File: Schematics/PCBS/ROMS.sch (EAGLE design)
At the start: 4 parts, among them IC1 ATMEGA328P-AU, Y1 16MHz

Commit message: working on VCC power
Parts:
- added R1: 10K, adafruit:R-US_0207/10
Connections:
- new net N$3: IC1.PC6_[RESET/PCINT14], R1.1
- new net VCC: IC1.AVCC, IC1.VCC_1, IC1.VCC_2, R1.2
- net GND: now also C1.2, IC1.GND_1, IC1.GND_2, IC1.GND_3; no longer C1.1
- net N$1: now also C1.1; no longer C1.2
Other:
- moved on the sheet: C1

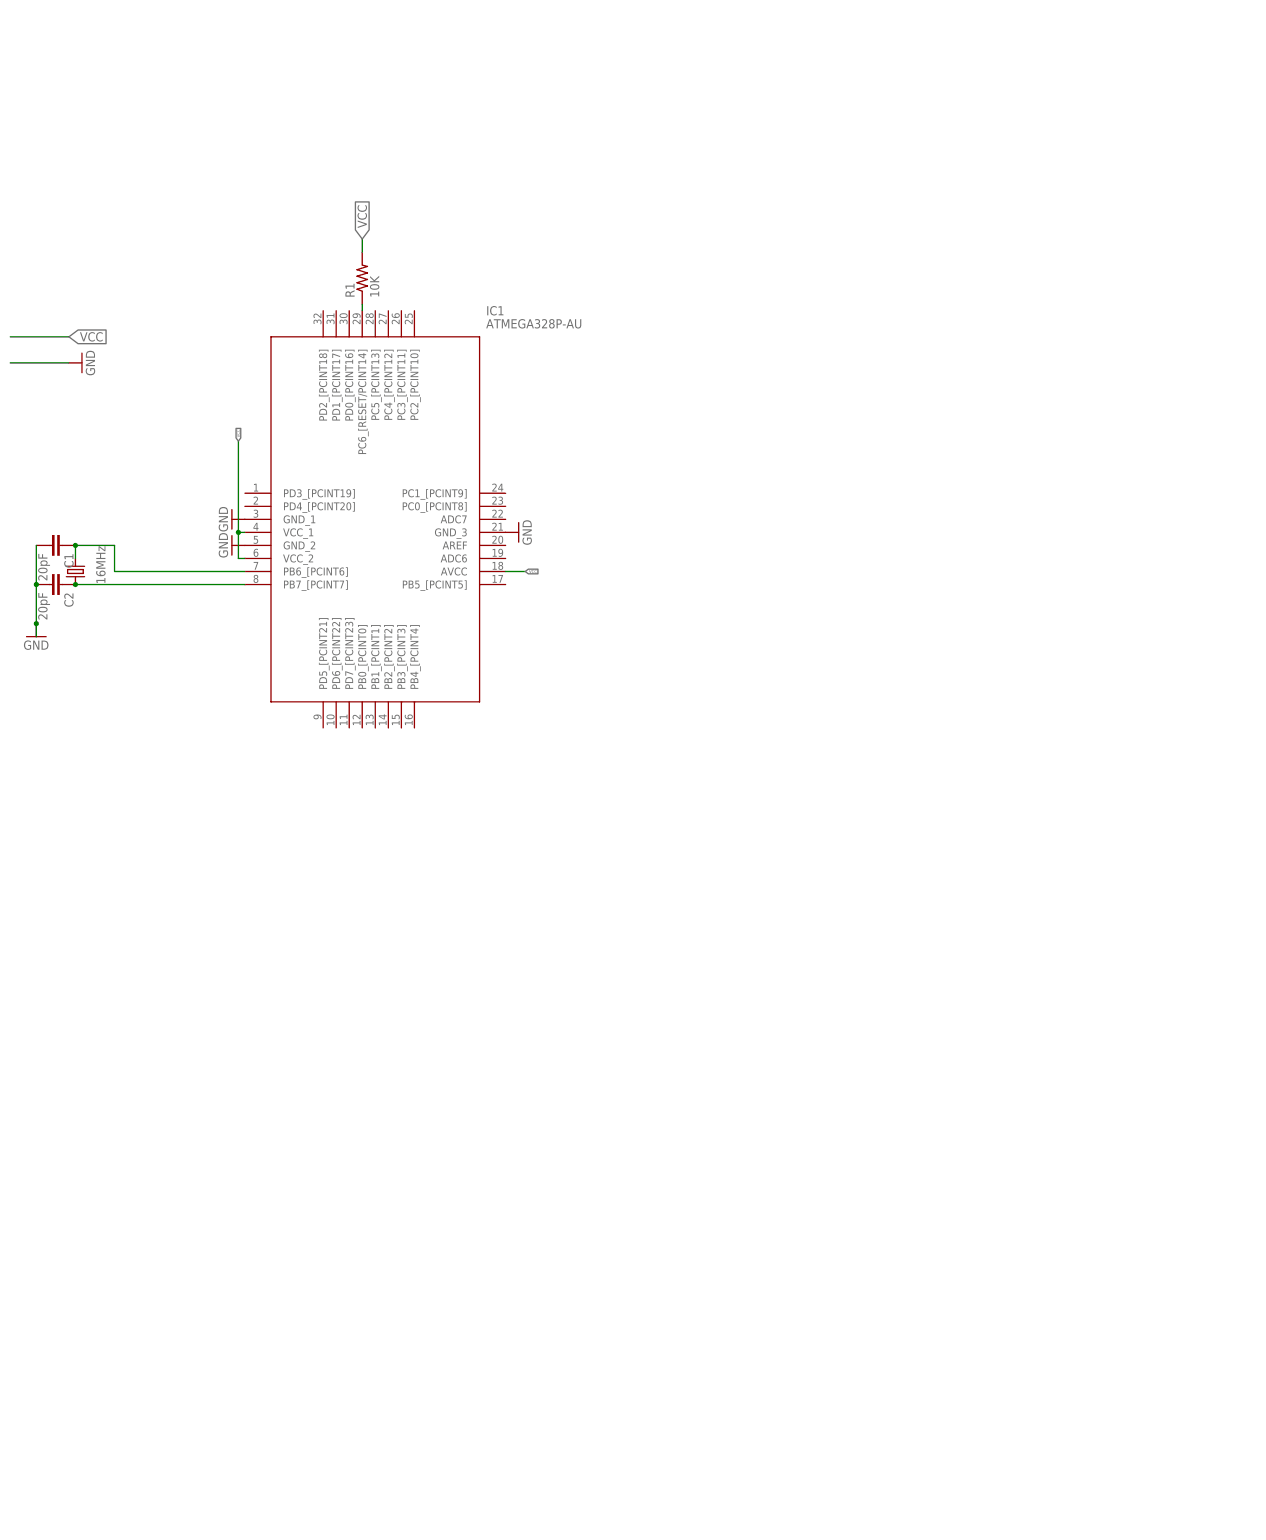
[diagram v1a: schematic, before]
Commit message: Start of NRF24lo1 hook up & LED’s
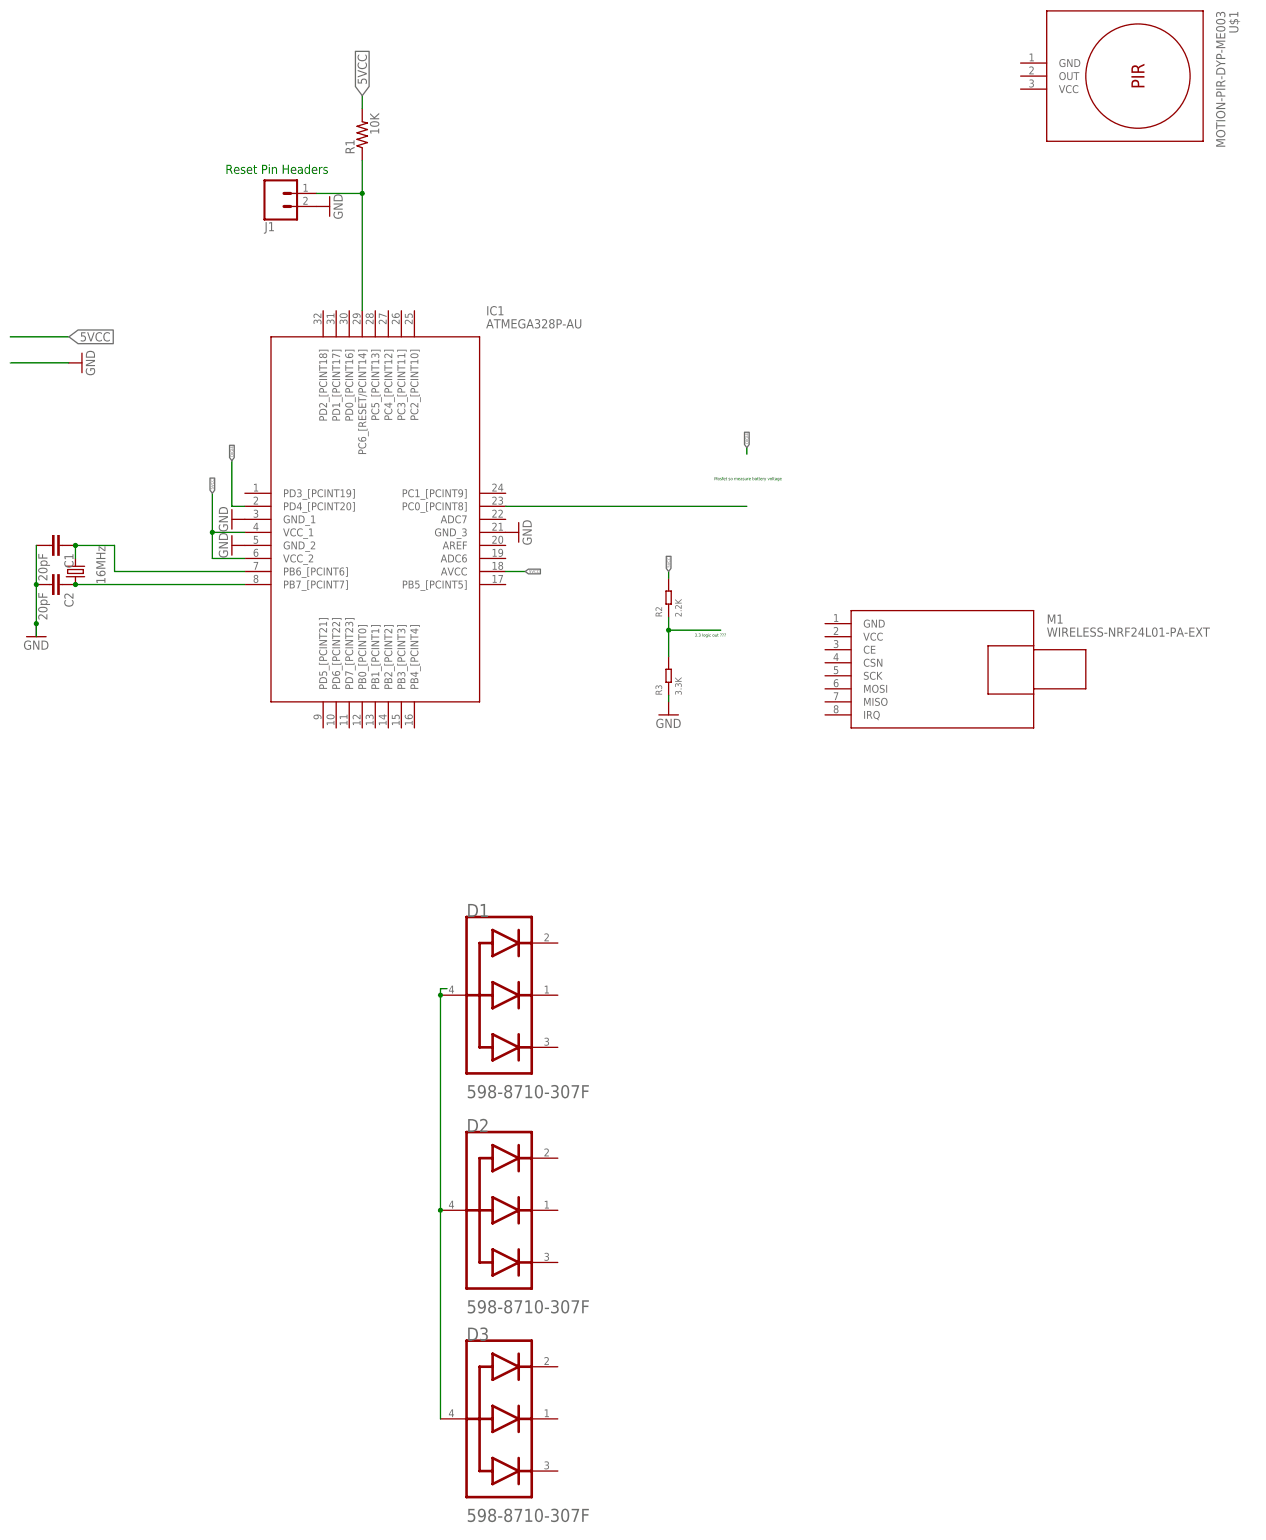
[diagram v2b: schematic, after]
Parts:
- added D1, D2, D3: DIALIGHT_598-8710-307FDIALIGHT_598-8710-307F_0_0, Dialight - 598-8710-307F:DIALIGHT_598-8710-307FDIALIGHT_598-8710-307F_0_0
- added J1: (no value), SparkFun-Connectors:CONN_02
- added M1: WIRELESS-NRF24L01-PA-EXT, diy-modules:WIRELESS-NRF24L01-PA-EXT
- added R2: 2.2K, Seeed-Resistor-2016:DIP-RES-2.2K-5%-1/4W(PR-D2.3XL6.5MM)
- added R3: 3.3K, Seeed-Resistor-2016:DIP-RES-3.3K-5%-1/4W(PR-D2.3XL6.5MM)
- added U$1: MOTION-PIR-DYP-ME003, diy-modules:MOTION-PIR-DYP-ME003
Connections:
- removed net VCC: IC1.AVCC, IC1.VCC_1, IC1.VCC_2, R1.2
- new net 5VCC: IC1.AVCC, IC1.VCC_1, IC1.VCC_2, R1.2, R2.2
- new net DIGI4: IC1.PD4_[PCINT20]
- new net N$4: IC1.PC0_[PCINT8]
- new net N$5: R2.1, R3.2
- new net N$6: D1.COMMON_ANODE, D2.COMMON_ANODE, D3.COMMON_ANODE
- net GND: now also J1.2, R3.1
- net N$3: now also J1.1
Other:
- note added: "3.3 logic out ???"
- note added: "Mosfet so measure battery voltage"
- note added: "Reset Pin Headers"
- moved on the sheet: R1

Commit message: removed LED from ROMS
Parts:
- removed D1, D2, D3: DIALIGHT_598-8710-307FDIALIGHT_598-8710-307F_0_0, Dialight - 598-8710-307F:DIALIGHT_598-8710-307FDIALIGHT_598-8710-307F_0_0
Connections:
- removed net N$6: D1.COMMON_ANODE, D2.COMMON_ANODE, D3.COMMON_ANODE
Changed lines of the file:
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@@
 <part name="U$1" library="diy-modules" deviceset="MOTION-PIR-DYP-ME003" device=""/>
 <part name="M1" library="diy-modules" deviceset="WIRELESS-NRF24L01-PA-EXT" device=""/>
-<part name="D1" library="Dialight - 598-8710-307F" deviceset="DIALIGHT_598-8710-307F" device="DIALIGHT_598-8710-307F_0_0"/>
-<part name="D2" library="Dialight - 598-8710-307F" deviceset="DIALIGHT_598-8710-307F" device="DIALIGHT_598-8710-307F_0_0"/>
-<part name="D3" library="Dialight - 598-8710-307F" deviceset="DIALIGHT_598-8710-307F" device="DIALIGHT_598-8710-307F_0_0"/>
 <part name="R2" library="Seeed-Resistor-2016" deviceset="DIP-RES-2.2K-5%-1/4W(PR-D2.3XL6.5MM)" device="" value="2.2K"/>
 <part name="R3" library="Seeed-Resistor-2016" deviceset="DIP-RES-3.3K-5%-1/4W(PR-D2.3XL6.5MM)" device="" value="3.3K"/>
@@
 <attribute name="VALUE" x="207.01" y="20.32" size="1.778" layer="96"/>
 </instance>
-<instance part="D1" gate="G$0" x="93.98" y="-29.21" smashed="yes">
-<attribute name="NAME" x="93.98" y="-31.75" size="2.54" layer="95" align="top-left"/>
-</instance>
-<instance part="D2" gate="G$0" x="93.98" y="-71.12" smashed="yes">
-<attribute name="NAME" x="93.98" y="-73.66" size="2.54" layer="95" align="top-left"/>
-</instance>
-<instance part="D3" gate="G$0" x="93.98" y="-111.76" smashed="yes">
-<attribute name="NAME" x="93.98" y="-114.3" size="2.54" layer="95" align="top-left"/>
-</instance>
 <instance part="R2" gate="G$1" x="133.35" y="27.94" smashed="yes" rot="R90">
 <attribute name="NAME" x="132.08" y="24.13" size="1.27" layer="95" ratio="10" rot="R90"/>
@@
 </segment>
 </net>
-<net name="N$6" class="0">
-<segment>
-<pinref part="D3" gate="G$0" pin="COMMON_ANODE"/>
-<wire x1="88.9" y1="-132.08" x2="88.9" y2="-91.44" width="0.1524" layer="91"/>
-<wire x1="88.9" y1="-91.44" x2="88.9" y2="-49.53" width="0.1524" layer="91"/>
-<wire x1="88.9" y1="-49.53" x2="88.9" y2="-48.26" width="0.1524" layer="91"/>
-<wire x1="88.9" y1="-48.26" x2="90.17" y2="-48.26" width="0.1524" layer="91"/>
-<pinref part="D2" gate="G$0" pin="COMMON_ANODE"/>
-<junction x="88.9" y="-91.44"/>
-<pinref part="D1" gate="G$0" pin="COMMON_ANODE"/>
-<junction x="88.9" y="-49.53"/>
-</segment>
-</net>

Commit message: led + atmega328
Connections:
- new net N$6: IC1.PB4_[PCINT4]
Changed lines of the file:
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@@
 <setting verticaltext="up"/>
 </settings>
-<grid distance="1.27" unitdist="mm" unit="mm" style="lines" multiple="1" display="no" altdistance="0.003125" altunitdist="mic" altunit="mm"/>
+<grid distance="0.1" unitdist="inch" unit="inch" style="lines" multiple="1" display="no" altdistance="0.01" altunitdist="inch" altunit="inch"/>
 <layers>
 <layer number="1" name="Top" color="4" fill="1" visible="no" active="no"/>
@@
 </segment>
 </net>
+<net name="N$6" class="0">
+<segment>
+<pinref part="IC1" gate="G$1" pin="PB4_[PCINT4]"/>
+<wire x1="83.82" y1="2.54" x2="83.82" y2="0" width="0.1524" layer="91"/>
+</segment>
+</net>

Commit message: Fix layout issues via fix to grid
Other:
- moved on the sheet: U$1
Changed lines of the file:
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@@
 <setting verticaltext="up"/>
 </settings>
-<grid distance="0.1" unitdist="inch" unit="inch" style="lines" multiple="1" display="no" altdistance="0.01" altunitdist="inch" altunit="inch"/>
+<grid distance="0.1" unitdist="inch" unit="inch" style="lines" multiple="1" display="yes" altdistance="0.01" altunitdist="inch" altunit="inch"/>
 <layers>
 <layer number="1" name="Top" color="4" fill="1" visible="no" active="no"/>
@@
 <attribute name="VALUE" x="69.85" y="101.6" size="1.778" layer="96" rot="R90"/>
 </instance>
-<instance part="U$1" gate="G$1" x="222.25" y="129.54" smashed="yes" rot="R270">
-<attribute name="NAME" x="242.57" y="142.24" size="1.778" layer="95" rot="R270"/>
-<attribute name="VALUE" x="240.03" y="142.24" size="1.778" layer="96" rot="R270"/>
+<instance part="U$1" gate="G$1" x="215.9" y="119.38" smashed="yes" rot="R270">
+<attribute name="NAME" x="236.22" y="132.08" size="1.778" layer="95" rot="R270"/>
+<attribute name="VALUE" x="233.68" y="132.08" size="1.778" layer="96" rot="R270"/>
 </instance>
 <instance part="M1" gate="G$1" x="186.69" y="12.7" smashed="yes">
@@
 <segment>
 <pinref part="IC1" gate="G$1" pin="VCC_2"/>
-<wire x1="50.8" y1="35.56" x2="44.45" y2="35.56" width="0.1524" layer="91"/>
-<wire x1="44.45" y1="35.56" x2="44.45" y2="40.64" width="0.1524" layer="91"/>
+<wire x1="50.8" y1="35.56" x2="43.18" y2="35.56" width="0.1524" layer="91"/>
+<wire x1="43.18" y1="35.56" x2="43.18" y2="40.64" width="0.1524" layer="91"/>
 <pinref part="IC1" gate="G$1" pin="VCC_1"/>
-<wire x1="44.45" y1="40.64" x2="44.45" y2="48.26" width="0.1524" layer="91"/>
-<wire x1="50.8" y1="40.64" x2="44.45" y2="40.64" width="0.1524" layer="91"/>
-<junction x="44.45" y="40.64"/>
-<label x="44.45" y="48.26" size="0.6096" layer="95" rot="R90" xref="yes"/>
-</segment>
-<segment>
+<wire x1="43.18" y1="40.64" x2="43.18" y2="48.26" width="0.1524" layer="91"/>
+<wire x1="50.8" y1="40.64" x2="43.18" y2="40.64" width="0.1524" layer="91"/>
+<junction x="43.18" y="40.64"/>
+<label x="43.18" y="48.26" size="0.6096" layer="95" rot="R90" xref="yes"/>
+</segment>
+<segment>
